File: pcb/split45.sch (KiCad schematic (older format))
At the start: 92 parts, among them U1 nice_nano, U2 nice_nano

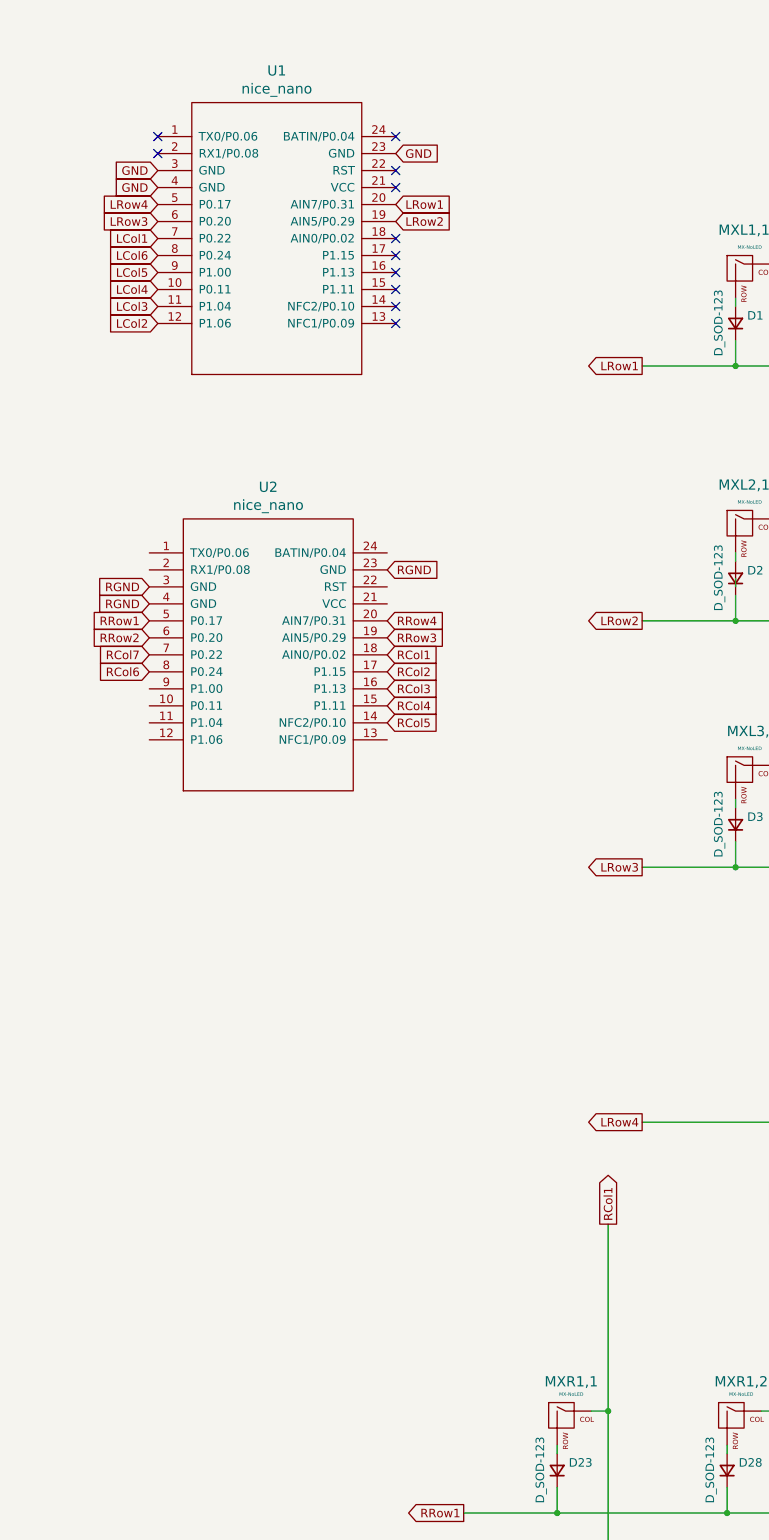
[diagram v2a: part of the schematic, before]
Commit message: add reset pads
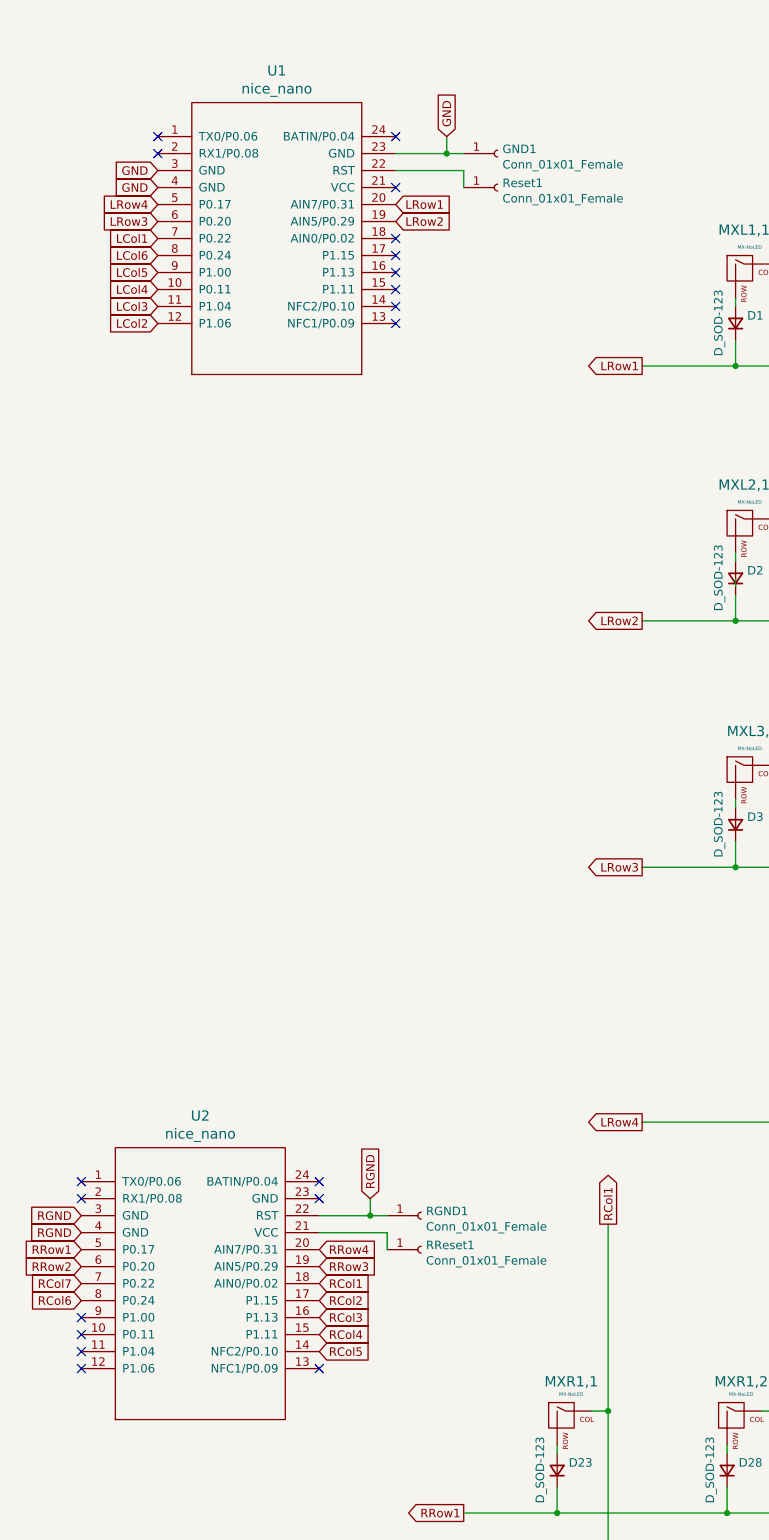
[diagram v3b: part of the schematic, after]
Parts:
- added GND1, RGND1, RReset1, Reset1: Conn_01x01_Female, Connector_Wire:SolderWire-0.15sqmm_1x01_D0.5mm_OD1.5mm, symbol Connector:Conn_01x01_Female
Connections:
- net GND: now also GND1.1 (Pin_1)
- net RGND: now also U2.22 (RST), RGND1.1 (Pin_1); no longer U2.23 (GND)
- net at U1.22 (RST): now also Reset1.1 (Pin_1)
- net at U2.21 (VCC): now also RReset1.1 (Pin_1)
- no-connect marks 11 -> 19
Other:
- moved on the sheet: U2
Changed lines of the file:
@@
 L nice_nano:nice_nano U2
 U 1 1 60F4CBBD
-P 2250 4700
-F 0 "U2" H 2250 5637 60  0000 C CNN
-F 1 "nice_nano" H 2250 5531 60  0000 C CNN
-F 2 "nice-nano-kicad:nice_nano" V 3300 2200 60  0001 C CNN
-F 3 "" V 3300 2200 60  0001 C CNN
-	1    2250 4700
+P 1850 8400
+F 0 "U2" H 1850 9337 60  0000 C CNN
+F 1 "nice_nano" H 1850 9231 60  0000 C CNN
+F 2 "nice-nano-kicad:nice_nano" V 2900 5900 60  0001 C CNN
+F 3 "" V 2900 5900 60  0001 C CNN
+	1    1850 8400
 	1    0    0    -1
 $EndComp
 NoConn ~ 3000 1700
-NoConn ~ 3000 1900
 NoConn ~ 3000 2000
 NoConn ~ 1600 1700
@@
 	1    0    0    -1
 $EndComp
-Text GLabel 3000 1800 2    50   Input ~ 0
+Text GLabel 3300 1700 1    50   Input ~ 0
 GND
 Text GLabel 1600 1900 0    50   Input ~ 0
@@
 Connection ~ 3950 14250
 Connection ~ 5950 14250
-Text GLabel 1550 4650 0    50   Input ~ 0
+Text GLabel 1150 8350 0    50   Input ~ 0
 RRow2
-Text GLabel 1550 4550 0    50   Input ~ 0
+Text GLabel 1150 8250 0    50   Input ~ 0
 RRow1
-Text GLabel 2950 4550 2    50   Input ~ 0
+Text GLabel 2550 8250 2    50   Input ~ 0
 RRow4
-Text GLabel 2950 4650 2    50   Input ~ 0
+Text GLabel 2550 8350 2    50   Input ~ 0
 RRow3
-Text GLabel 1550 4750 0    50   Input ~ 0
+Text GLabel 1150 8450 0    50   Input ~ 0
 RCol7
-Text GLabel 1550 4850 0    50   Input ~ 0
+Text GLabel 1150 8550 0    50   Input ~ 0
 RCol6
-Text GLabel 2950 4750 2    50   Input ~ 0
+Text GLabel 2550 8450 2    50   Input ~ 0
 RCol1
-Text GLabel 2950 4850 2    50   Input ~ 0
+Text GLabel 2550 8550 2    50   Input ~ 0
 RCol2
-Text GLabel 2950 4950 2    50   Input ~ 0
+Text GLabel 2550 8650 2    50   Input ~ 0
 RCol3
-Text GLabel 2950 5050 2    50   Input ~ 0
+Text GLabel 2550 8750 2    50   Input ~ 0
 RCol4
-Text GLabel 2950 5150 2    50   Input ~ 0
+Text GLabel 2550 8850 2    50   Input ~ 0
 RCol5
-Text GLabel 1550 4350 0    50   Input ~ 0
+Text GLabel 1150 8050 0    50   Input ~ 0
 RGND
-Text GLabel 1550 4450 0    50   Input ~ 0
+Text GLabel 1150 8150 0    50   Input ~ 0
 RGND
-Text GLabel 2950 4250 2    50   Input ~ 0
+$Comp
+L Connector:Conn_01x01_Female Reset1
+U 1 1 6078C771
+P 3600 2000
+F 0 "Reset1" H 3628 2026 50  0000 L CNN
+F 1 "Conn_01x01_Female" H 3628 1935 50  0000 L CNN
+F 2 "Connector_Wire:SolderWire-0.15sqmm_1x01_D0.5mm_OD1.5mm" H 3600 2000 50  0001 C CNN
+F 3 "~" H 3600 2000 50  0001 C CNN
+	1    3600 2000
+	1    0    0    -1
+$EndComp
+$Comp
+L Connector:Conn_01x01_Female GND1
+U 1 1 6079FD38
+P 3600 1800
+F 0 "GND1" H 3628 1826 50  0000 L CNN
+F 1 "Conn_01x01_Female" H 3628 1735 50  0000 L CNN
+F 2 "Connector_Wire:SolderWire-0.15sqmm_1x01_D0.5mm_OD1.5mm" H 3600 1800 50  0001 C CNN
+F 3 "~" H 3600 1800 50  0001 C CNN
+	1    3600 1800
+	1    0    0    -1
+$EndComp
+Wire Wire Line
+	3400 1900 3400 2000
+Wire Wire Line
+	3000 1900 3400 1900
+Wire Wire Line
+	3000 1800 3300 1800
+Wire Wire Line
+	3300 1800 3300 1700
+Connection ~ 3300 1800
+Wire Wire Line
+	3300 1800 3400 1800
+Text GLabel 2850 7950 1    50   Input ~ 0
 RGND
+$Comp
+L Connector:Conn_01x01_Female RReset1
+U 1 1 607FD244
+P 3150 8250
+F 0 "RReset1" H 3178 8276 50  0000 L CNN
+F 1 "Conn_01x01_Female" H 3178 8185 50  0000 L CNN
+F 2 "Connector_Wire:SolderWire-0.15sqmm_1x01_D0.5mm_OD1.5mm" H 3150 8250 50  0001 C CNN
+F 3 "~" H 3150 8250 50  0001 C CNN
+	1    3150 8250
+	1    0    0    -1
+$EndComp
+$Comp
+L Connector:Conn_01x01_Female RGND1
+U 1 1 607FD24A
+P 3150 8050
+F 0 "RGND1" H 3178 8076 50  0000 L CNN
+F 1 "Conn_01x01_Female" H 3178 7985 50  0000 L CNN
+F 2 "Connector_Wire:SolderWire-0.15sqmm_1x01_D0.5mm_OD1.5mm" H 3150 8050 50  0001 C CNN
+F 3 "~" H 3150 8050 50  0001 C CNN
+	1    3150 8050
+	1    0    0    -1
+$EndComp
+Wire Wire Line
+	2950 8150 2950 8250
+Wire Wire Line
+	2550 8150 2950 8150
+Wire Wire Line
+	2550 8050 2850 8050
+Wire Wire Line
+	2850 8050 2850 7950
+Connection ~ 2850 8050
+Wire Wire Line
+	2850 8050 2950 8050
+NoConn ~ 2550 7850
+NoConn ~ 2550 7950
+NoConn ~ 2550 8950
+NoConn ~ 1150 8950
+NoConn ~ 1150 8850
+NoConn ~ 1150 8750
+NoConn ~ 1150 8650
+NoConn ~ 1150 7950
+NoConn ~ 1150 7850
 $EndSCHEMATC
